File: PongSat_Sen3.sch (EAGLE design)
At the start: 28 parts, among them U1 MIC5129 3v3, U2 Micro SD, X1 USB-MICROB, Y1 8MHz

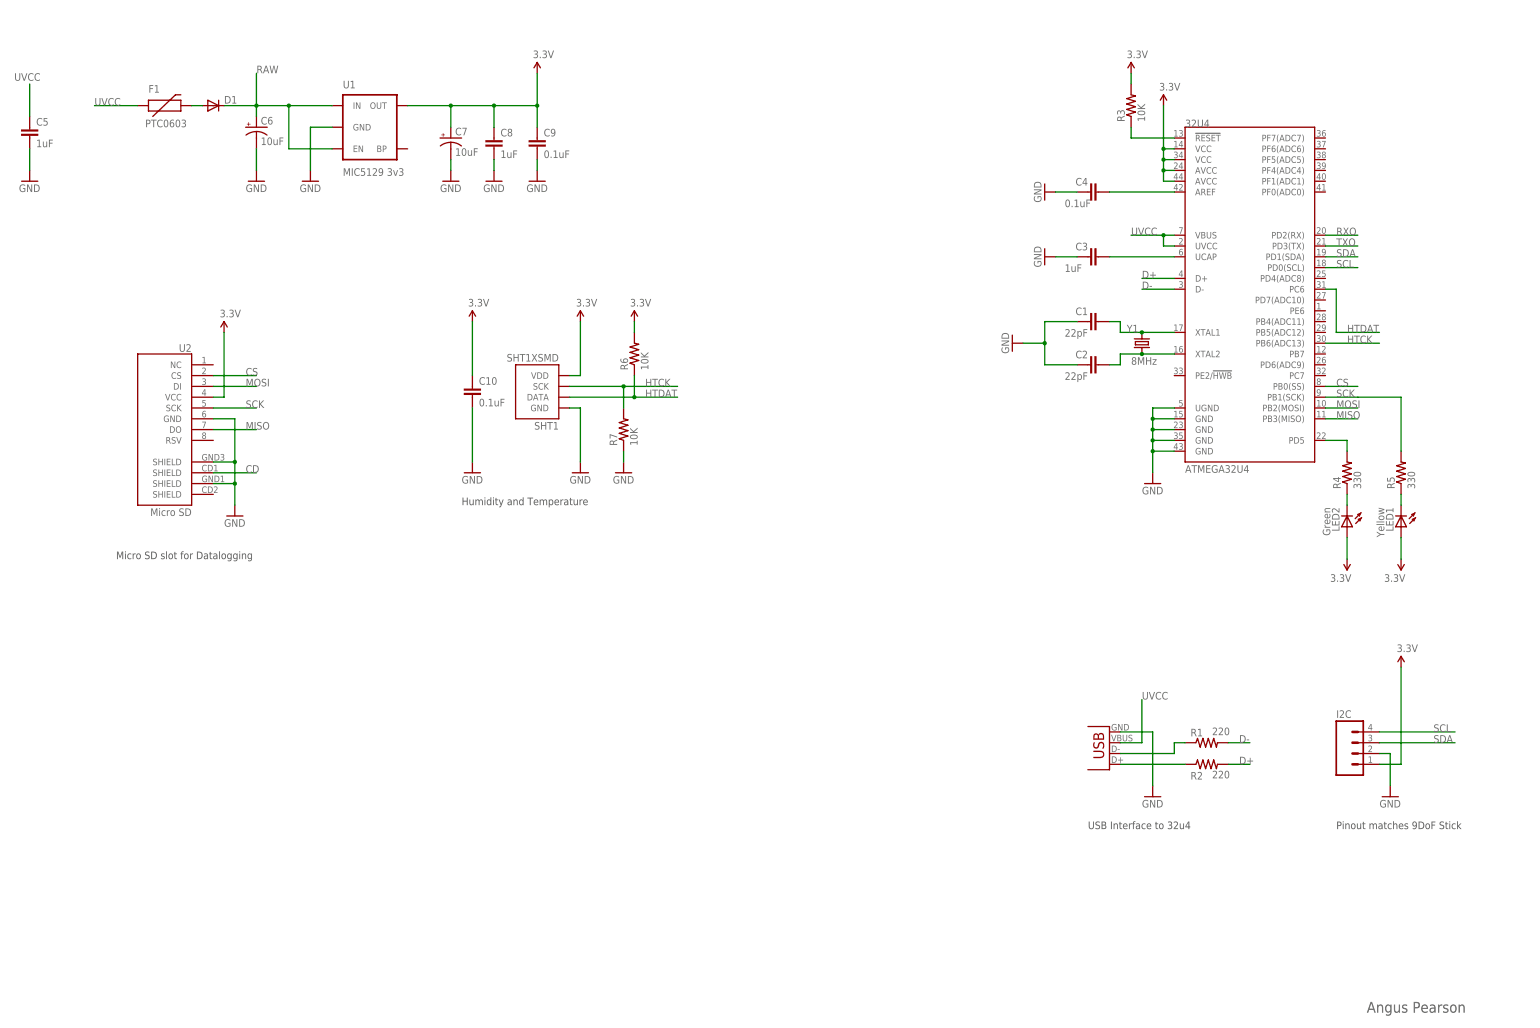
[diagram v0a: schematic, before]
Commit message: Updated PCB
Completed PCB (V3 BETA) uploaded. PCB is now produceable, but not ERC'd
or DRC'd.
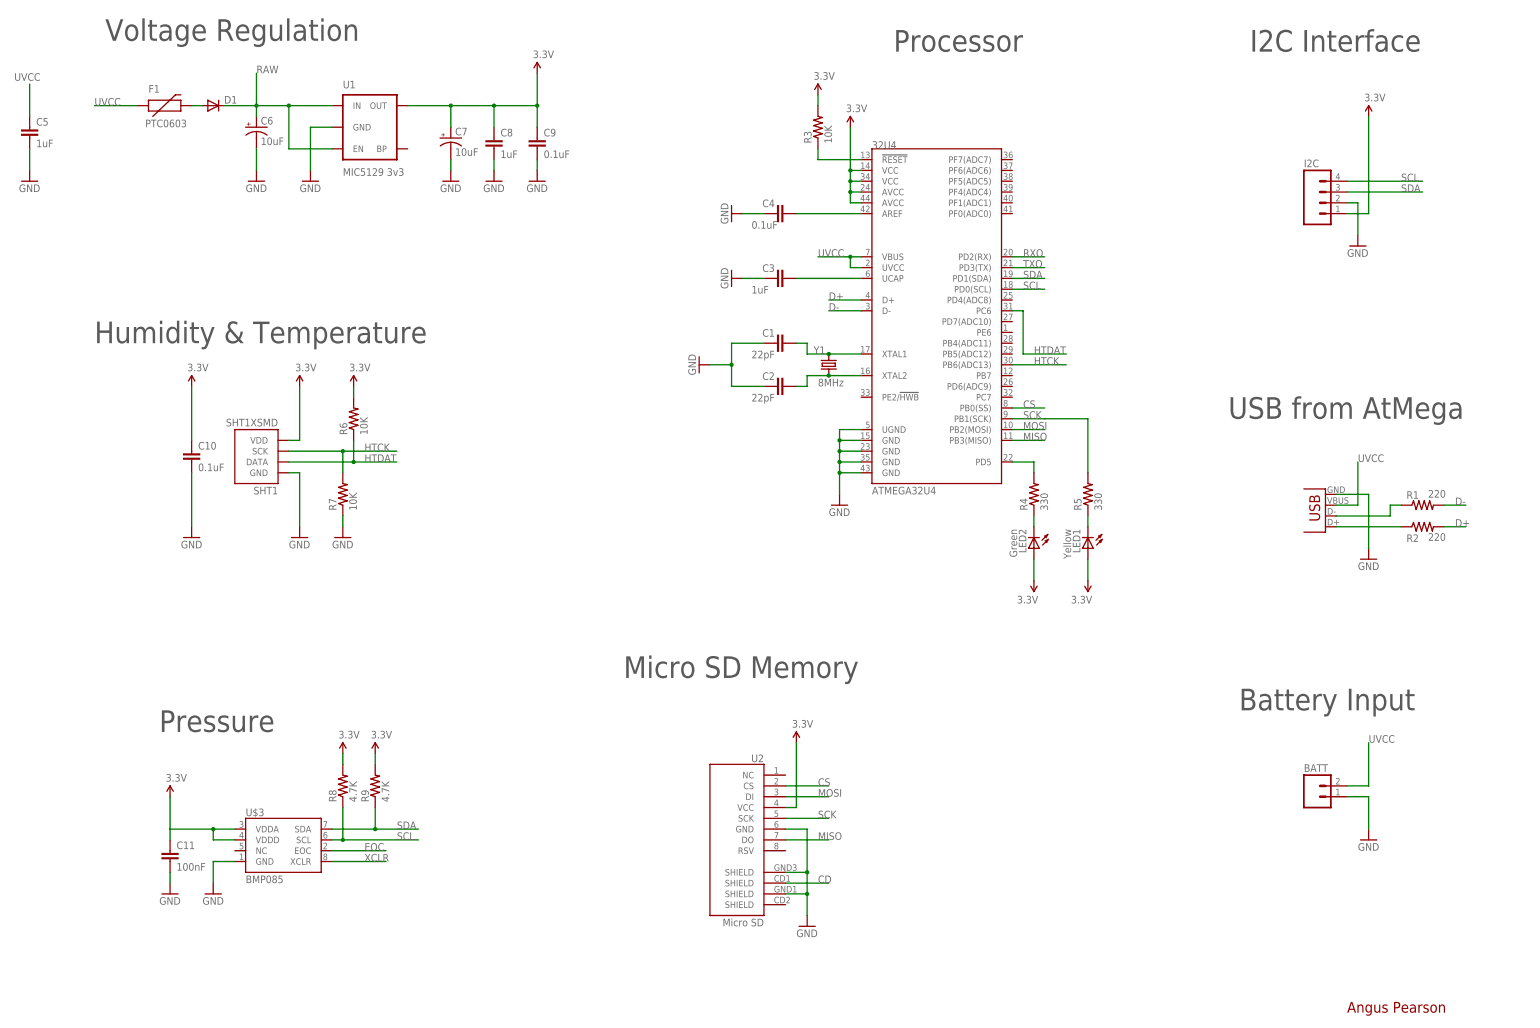
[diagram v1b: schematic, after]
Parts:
- added BATT: (no value), SparkFun-Connectors:M02PTH
- added C11: 100nF, SparkFun-Passives:CAP0402-CAP
- added R8, R9: 4.7K, SparkFun-Passives:RESISTOR0402-RES
- added U$3: BMP085, SparkFun-Sensors:BMP085
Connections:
- new net EOC: U$3.EOC
- new net XCLR: U$3.XCLR
- net 3.3V: now also C11.1, R8.2, R9.2, U$3.VDDA, U$3.VDDD
- net GND: now also BATT.1, C11.2, U$3.GND
- net SCL: now also R8.1, U$3.SCL
- net SDA: now also R9.1, U$3.SDA
- net UVCC: now also BATT.2
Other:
- note added: "Battery Input"
- note added: "Humidity & Temperature"
- note added: "I2C Interface"
- note added: "Micro SD Memory"
- note added: "Pressure"
- note added: "Processor"
- note added: "USB from AtMega"
- note added: "Voltage Regulation"
- note removed: "Humidity and Temperature"
- note removed: "Micro SD slot for Datalogging"
- note removed: "Pinout matches 9DoF Stick"
- note removed: "USB Interface to 32u4"
- moved on the sheet: 32U4, C1, C10, C2, C3, C4, I2C, LED1, LED2, R1, R2, R3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

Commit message: PCB Update
Updated PCB with SD fix and also added new Schematics to repo.
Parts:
- renumbered SHT1 to SHT, U$3 to BMP
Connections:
- net CD: now also 32U4.PC6
- net HTDAT: now also 32U4.PC7; no longer 32U4.PC6
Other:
- moved on the sheet: C5, C6, C7, C8, C9, D1, F1, U1

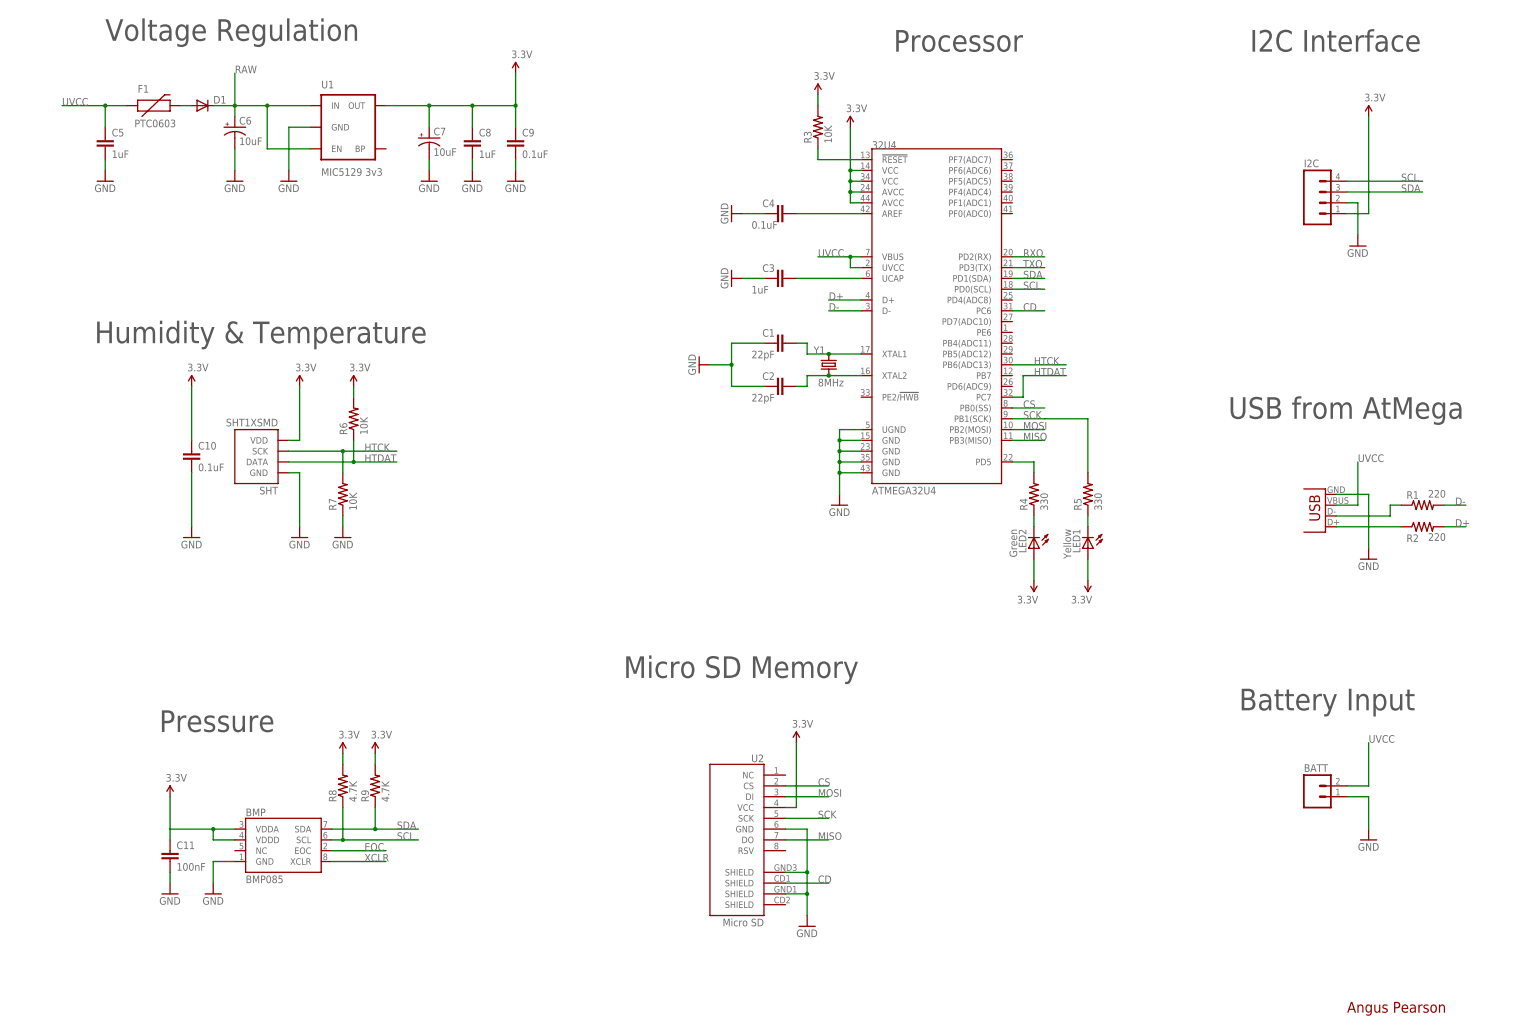
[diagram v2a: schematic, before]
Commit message: Updated PCB V3 Rev 3
Updated PCB with new Silkscreen, improved routing and placement, bias
and mounting holes. Included Schematics, PCB Printouts and Assembly
diagrams in repo :-)
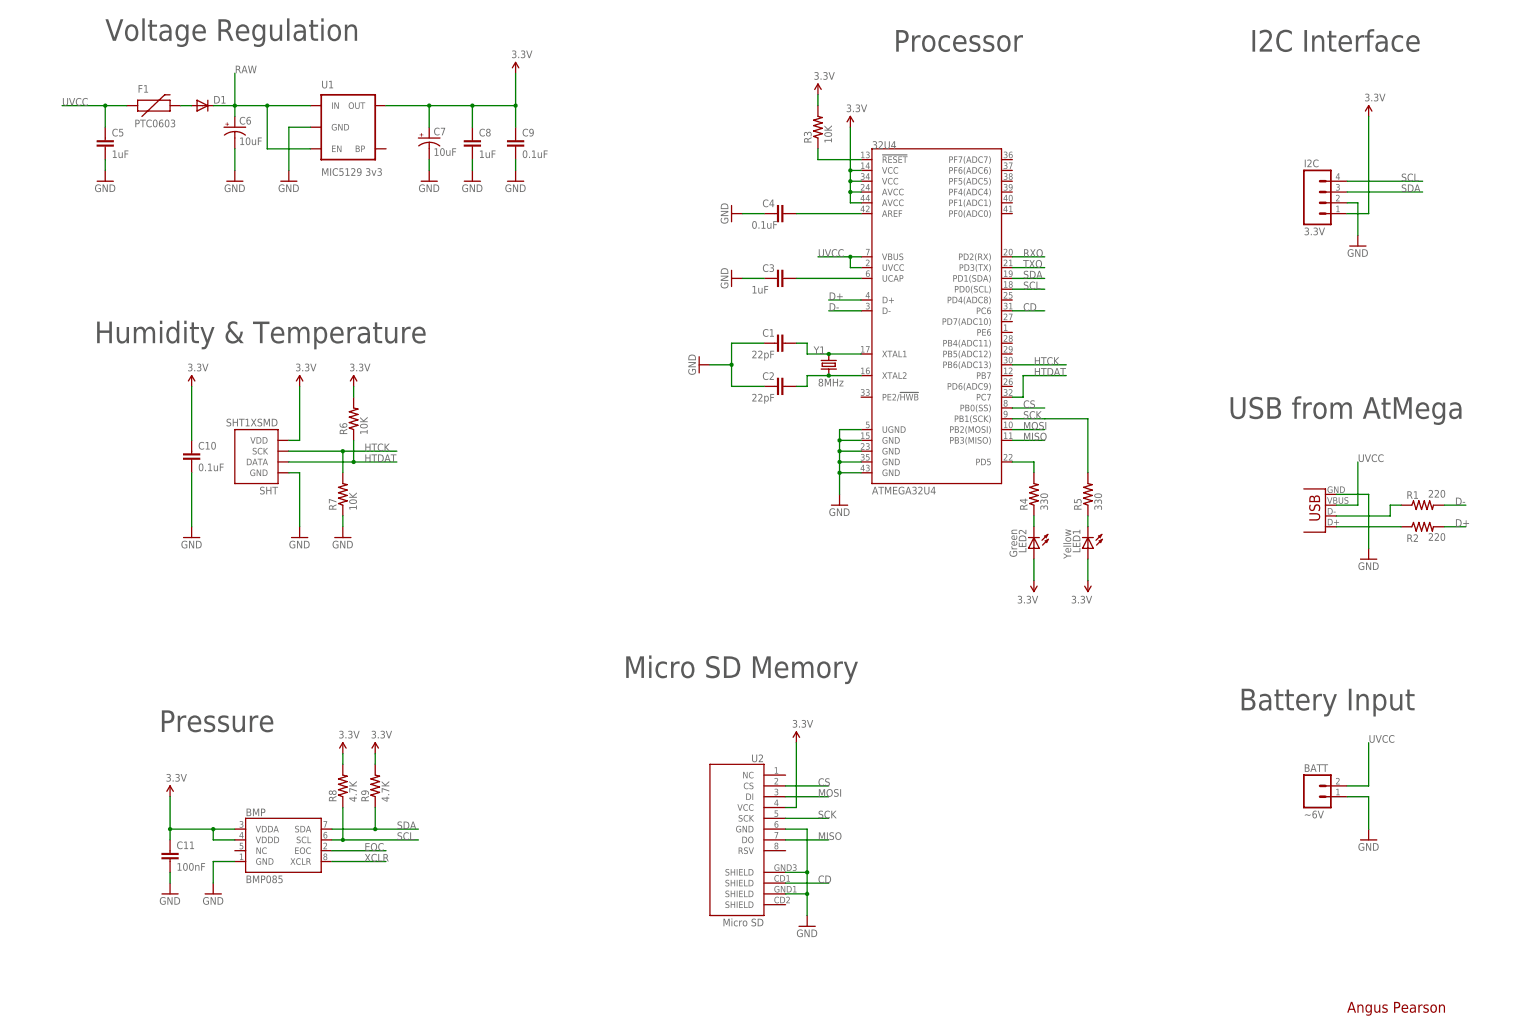
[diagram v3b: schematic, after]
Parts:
- BATT: value (none) -> ~6V
- I2C: value (none) -> 3.3V
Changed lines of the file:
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@@
 <part name="GND12" library="SparkFun-Aesthetics" deviceset="GND" device=""/>
 <part name="P+6" library="SparkFun-Aesthetics" deviceset="3.3V" device=""/>
-<part name="I2C" library="SparkFun-Connectors" deviceset="M04" device="SMD"/>
+<part name="I2C" library="SparkFun-Connectors" deviceset="M04" device="SMD" value="3.3V"/>
 <part name="P+7" library="SparkFun-Aesthetics" deviceset="3.3V" device=""/>
 <part name="GND13" library="SparkFun-Aesthetics" deviceset="GND" device=""/>
@@
 <part name="C11" library="SparkFun-Passives" deviceset="CAP" device="0402-CAP" value="100nF"/>
 <part name="GND18" library="SparkFun-Aesthetics" deviceset="GND" device=""/>
-<part name="BATT" library="SparkFun-Connectors" deviceset="M02" device="PTH"/>
+<part name="BATT" library="SparkFun-Connectors" deviceset="M02" device="PTH" value="~6V"/>
 <part name="GND19" library="SparkFun-Aesthetics" deviceset="GND" device=""/>
 </parts>
@@
 <pinref part="C11" gate="G$1" pin="1"/>
 <wire x1="55.88" y1="48.26" x2="55.88" y2="45.72" width="0.2032" layer="91"/>
+<junction x="55.88" y="48.26"/>
 </segment>
 <segment>
@@
 </sheet>
 </sheets>
+<errors>
+</errors>
 </schematic>
 </drawing>
